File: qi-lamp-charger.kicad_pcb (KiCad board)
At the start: 2 copper layers, 41.5 x 44 mm, 82 parts, among them J1 Conn_01x03, J2 Conn_01x02, J4 Conn_01x06, J5 Conn_01x03, Q1 BSS308PE H6327, SW1 SKTDLDE010, U1 SLG5NV1430V, U2 BQ51050BRHL, U3 ESP-12E

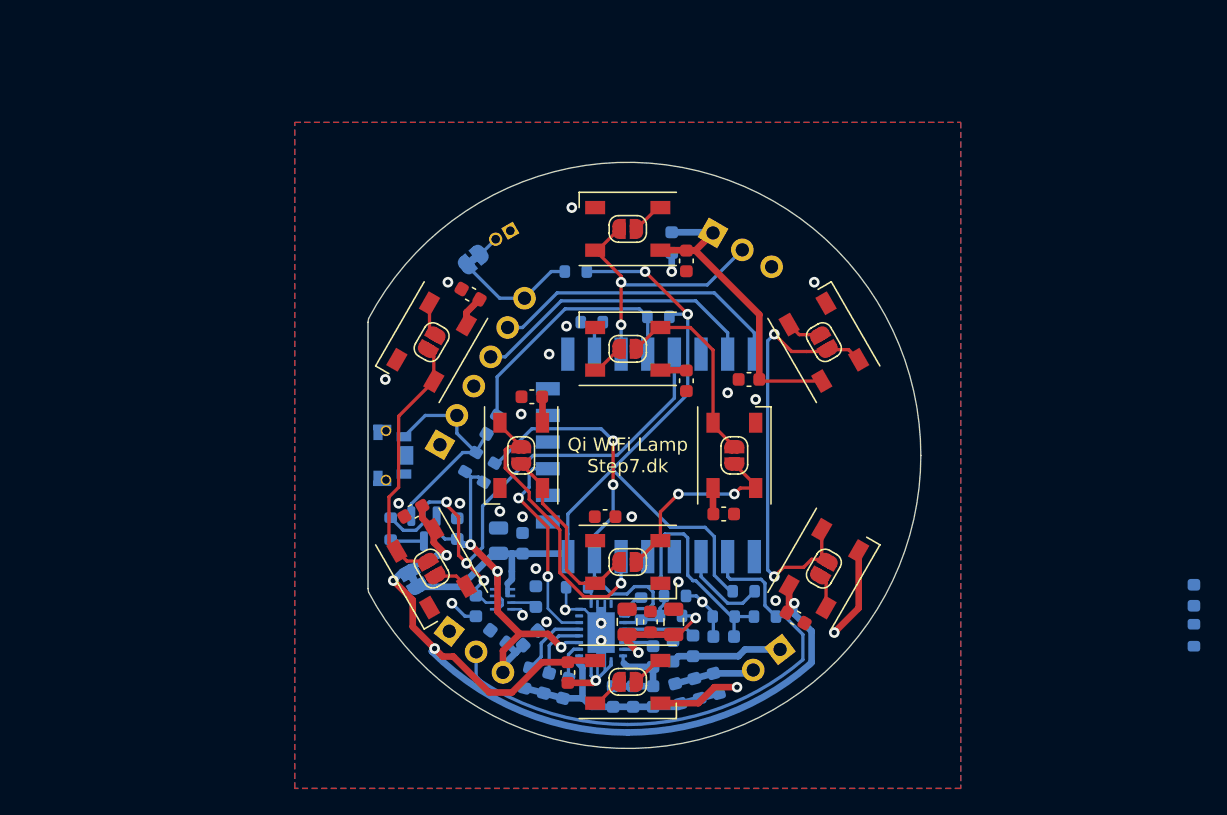
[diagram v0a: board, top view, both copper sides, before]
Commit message: Puzzle #4 - has GPIO0 brainfart
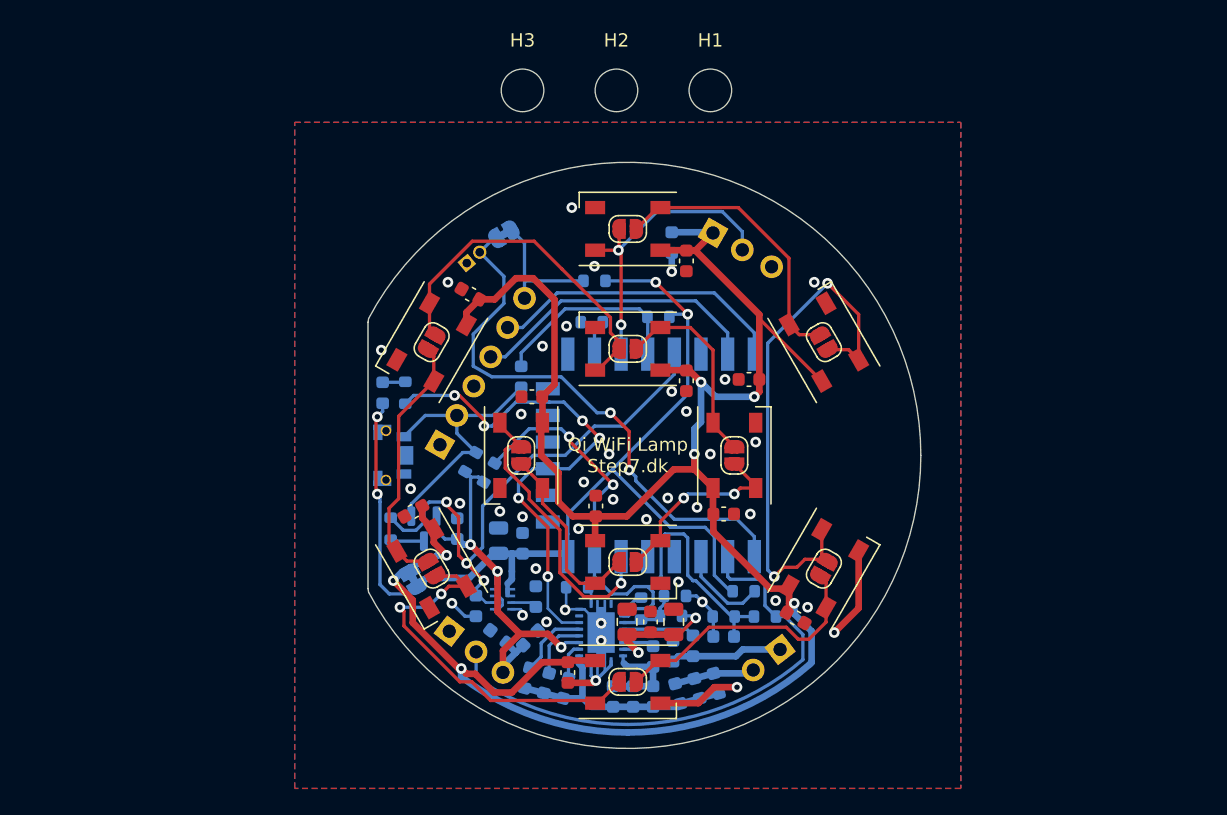
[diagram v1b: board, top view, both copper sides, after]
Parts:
- added H1: MountingHole, MountingHole:MountingHole_3.2mm_M3_ISO14580, F.Cu at (106.2, 72.6)
- added H2: MountingHole, MountingHole:MountingHole_3.2mm_M3_ISO14580, F.Cu at (99.2, 72.6)
- added H3: MountingHole, MountingHole:MountingHole_3.2mm_M3_ISO14580, F.Cu at (92.1, 72.6)
- moved D11 62.8 mm to (81.6, 95.3), turned to -90 degrees
- moved R4 61.9 mm to (83.3, 95.3)
- moved D12 4.22 mm to (92.0, 94.1), turned to 90 degrees
- moved TP1 4.07 mm to (87.9, 85.6), turned to -50 degrees
- moved JP12 2.98 mm to (90.7, 83.4), turned to 30 degrees
- moved R10 1.57 mm to (97.5, 86.9)
- moved C32 1.06 mm to (97.6, 103.8), turned to -90 degrees
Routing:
- net LED_V+: track 101.3 -> 160.8 mm, vias 4 -> 7
- net ~{ESP_RST}: track 1.65 -> 41.7 mm, vias 0 -> 2
- net Net-(D4-Pad4): track 5.06 -> 29.0 mm, vias 0 -> 2
- net ~{Qi_CHG/LED}: track 15.8 -> 38.6 mm, vias 2 -> 6
- net Net-(D6-Pad4): track 5.02 -> 26.4 mm
- net Net-(D1-Pad4): track 5.06 -> 21.3 mm
- net +VSW: track 62.3 -> 77.9 mm, vias 2 -> 4
- net Net-(D3-Pad4): track 5.02 -> 20.5 mm
- net Net-(D2-Pad4): track 33.1 -> 40.6 mm
- net ESP_GPIO0: track 19.4 -> 14.9 mm
- net DTR: track 17.0 -> 21.1 mm
- net LED_DIN: track 21.3 -> 23.7 mm
- net Net-(D11-Pad1): track 0.00 -> 1.72 mm
- net Qi_TS/CTRL: track 47.0 -> 45.4 mm
- net PWR_ON/~{OFF}: track 42.0 -> 40.9 mm
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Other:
- board text added: "GND DTR n/c TXD RXD RTS"
- board text added: "GND D_{in} V+"

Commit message: Puzzle #5
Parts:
- R10, R11, R12, R13, R9: value 10k -> 20k
- R14: value 1M -> 20k
- moved J5 5.11 mm to (110.8, 85.9), turned to 60 degrees
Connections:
- J5 pad 1: LED_V+ -> GND
- J5 pad 3: GND -> LED_V+
- Q1 pad 1: DTR -> BTN
- R14 pad 1: DTR -> BTN
- SW1 pad 2: DTR -> BTN
- U3 pad 5: unconnected-(U3-Pad5) -> BTN
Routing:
- net DTR: track 21.1 -> 5.71 mm
- net BTN: track 0.00 -> 13.9 mm
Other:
- board text added: "r${REVISION} Qi WiFi Lamp Step7.dk Martin Axelsen"
- board text removed: "Qi WiFi Lamp Step7.dk"
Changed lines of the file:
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@@
   )
   (paper "A4")
+  (title_block
+    (date "2022-05-20")
+    (rev "1.0.0")
+  )
   (layers
     (0 "F.Cu" signal)
@@
   (net 40 "Net-(R13-Pad2)")
   (net 41 "unconnected-(U3-Pad4)")
-  (net 42 "unconnected-(U3-Pad5)")
+  (net 42 "BTN")
   (net 43 "unconnected-(U3-Pad9)")
   (net 44 "unconnected-(U3-Pad10)")
@@
       (effects (font (size 1 1) (thickness 0.15)) (justify mirror))
     )
-    (fp_text value "10k" (at 0 -1.43) (layer "B.Fab") hide
+    (fp_text value "20k" (at 0 -1.43) (layer "B.Fab") hide
       (effects (font (size 1 1) (thickness 0.15)) (justify mirror))
     )
@@
       (net 41 "unconnected-(U3-Pad4)") (pinfunction "GPIO16") (pintype "bidirectional+no_connect"))
     (pad "5" smd rect (at -7.6 -4.5 90) (size 2.5 1) (layers "B.Cu" "B.Paste" "B.Mask")
-      (net 42 "unconnected-(U3-Pad5)") (pinfunction "GPIO14") (pintype "bidirectional+no_connect"))
+      (net 42 "BTN") (pinfunction "GPIO14") (pintype "bidirectional"))
     (pad "6" smd rect (at -7.6 -6.5 90) (size 2.5 1) (layers "B.Cu" "B.Paste" "B.Mask")
       (net 28 "LED_DOUT") (pinfunction "GPIO12") (pintype "bidirectional"))
@@
   )
   (footprint "Connector_PinHeader_2.54mm:PinHeader_1x03_P2.54mm_Vertical" (layer "B.Cu")
-    (at 106.4 83.3 -120)
+    (at 110.8 85.9 60)
     (descr "Through hole straight pin header, 1x03, 2.54mm pitch, single row")
     (tags "Through hole pin header THT 1x03 2.54mm single row")
@@
       (effects (font (size 1 1) (thickness 0.15)) (justify mirror))
     )
-    (fp_text user "Ext.LED" (at -3.001666 -2.539039 -30) (layer "B.SilkS")
+    (fp_text user "Ext.LED" (at 3.251666 -2.10795 150) (layer "B.SilkS")
       (effects (font (size 1 1) (thickness 0.15)) (justify mirror))
     )
@@
     (fp_line (start 1.27 -6.35) (end -1.27 -6.35) (layer "B.Fab") (width 0.1))
     (fp_line (start -0.635 1.27) (end 1.27 1.27) (layer "B.Fab") (width 0.1))
-    (pad "1" thru_hole rect (at 0 0 240) (size 1.7 1.7) (drill 1) (layers *.Cu *.Mask)
-      (net 23 "LED_V+") (pinfunction "Pin_1") (pintype "passive"))
-    (pad "2" thru_hole oval (at 0 -2.54 240) (size 1.7 1.7) (drill 1) (layers *.Cu *.Mask)
+    (pad "1" thru_hole rect (at 0 0 60) (size 1.7 1.7) (drill 1) (layers *.Cu *.Mask)
+      (net 5 "GND") (pinfunction "Pin_1") (pintype "passive"))
+    (pad "2" thru_hole oval (at 0 -2.54 60) (size 1.7 1.7) (drill 1) (layers *.Cu *.Mask)
       (net 24 "LED_DIN") (pinfunction "Pin_2") (pintype "passive"))
-    (pad "3" thru_hole oval (at 0 -5.08 240) (size 1.7 1.7) (drill 1) (layers *.Cu *.Mask)
-      (net 5 "GND") (pinfunction "Pin_3") (pintype "passive"))
+    (pad "3" thru_hole oval (at 0 -5.08 60) (size 1.7 1.7) (drill 1) (layers *.Cu *.Mask)
+      (net 23 "LED_V+") (pinfunction "Pin_3") (pintype "passive"))
     (model "${KICAD6_3DMODEL_DIR}/Connector_PinHeader_2.54mm.3dshapes/PinHeader_1x03_P2.54mm_Vertical.wrl" hide
       (offset (xyz 0 0 0))
@@
       (effects (font (size 1 1) (thickness 0.15)) (justify mirror))
     )
-    (fp_text value "10k" (at 0 -1.43) (layer "B.Fab") hide
+    (fp_text value "20k" (at 0 -1.43) (layer "B.Fab") hide
       (effects (font (size 1 1) (thickness 0.15)) (justify mirror))
     )
@@
       (effects (font (size 1 1) (thickness 0.15)) (justify mirror))
     )
-    (fp_text value "10k" (at 0 -1.43 90) (layer "B.Fab") hide
+    (fp_text value "20k" (at 0 -1.43 90) (layer "B.Fab") hide
       (effects (font (size 1 1) (thickness 0.15)) (justify mirror))
     )
@@
       (effects (font (size 1 1) (thickness 0.15)) (justify mirror))
     )
-    (fp_text value "10k" (at 0 -1.43) (layer "B.Fab") hide
+    (fp_text value "20k" (at 0 -1.43) (layer "B.Fab") hide
       (effects (font (size 1 1) (thickness 0.15)) (justify mirror))
     )
@@
       (net 5 "GND") (pinfunction "1") (pintype "passive"))
     (pad "2" smd rect locked (at 1.4 1.35 90) (size 0.7 1.1) (layers "B.Cu" "B.Paste" "B.Mask")
-      (net 29 "DTR") (pinfunction "2") (pintype "passive"))
+      (net 42 "BTN") (pinfunction "2") (pintype "passive"))
     (pad "3" smd rect locked (at 0 1.5 90) (size 1.4 1.1) (layers "B.Cu" "B.Paste" "B.Mask")
       (net 5 "GND") (pintype "passive"))
@@
       (effects (font (size 1 1) (thickness 0.15)) (justify mirror))
     )
-    (fp_text value "1M" (at 0 -1.43 60) (layer "B.Fab") hide
+    (fp_text value "20k" (at 0 -1.43 60) (layer "B.Fab") hide
       (effects (font (size 1 1) (thickness 0.15)) (justify mirror))
     )
@@
     (fp_line (start -0.8 -0.4125) (end -0.8 0.4125) (layer "B.Fab") (width 0.1))
     (pad "1" smd roundrect (at -0.825 0 240) (size 0.8 0.95) (layers "B.Cu" "B.Paste" "B.Mask") (roundrect_rratio 0.25)
-      (net 29 "DTR") (pintype "passive"))
+      (net 42 "BTN") (pintype "passive"))
     (pad "2" smd roundrect (at 0.825 0 240) (size 0.8 0.95) (layers "B.Cu" "B.Paste" "B.Mask") (roundrect_rratio 0.25)
       (net 6 "+BATT") (pintype "passive"))
@@
       (effects (font (size 1 1) (thickness 0.15)) (justify mirror))
     )
-    (fp_text value "10k" (at 0 -1.43) (layer "B.Fab") hide
+    (fp_text value "20k" (at 0 -1.43) (layer "B.Fab") hide
       (effects (font (size 1 1) (thickness 0.15)) (justify mirror))
     )
@@
     (fp_line (start 0.65 1.45) (end 0.65 -1.45) (layer "B.Fab") (width 0.1))
     (pad "1" smd roundrect (at -0.9375 0.95 270) (size 1.475 0.6) (layers "B.Cu" "B.Paste" "B.Mask") (roundrect_rratio 0.25)
-      (net 29 "DTR") (pinfunction "G") (pintype "input"))
+      (net 42 "BTN") (pinfunction "G") (pintype "input"))
     (pad "2" smd roundrect (at -0.9375 -0.95 270) (size 1.475 0.6) (layers "B.Cu" "B.Paste" "B.Mask") (roundrect_rratio 0.25)
       (net 6 "+BATT") (pinfunction "S") (pintype "passive"))
@@
     (effects (font (size 1 1) (thickness 0.15)) (justify mirror))
   )
-  (gr_text "Qi WiFi Lamp\nStep7.dk" (at 100 100) (layer "F.SilkS")
+  (gr_text "r${REVISION}\nQi WiFi Lamp\nStep7.dk\n\nMartin Axelsen" (at 115.75 100 270) (layer "F.SilkS")
     (effects (font (size 1 1) (thickness 0.15)))
   )
@@
   (via (at 99.5 109.6) (size 0.8) (drill 0.4) (layers "F.Cu" "B.Cu") (net 28))
   (segment (start 99.5 109.6) (end 99.5 107.6) (width 0.25) (layer "B.Cu") (net 28))
-  (segment (start 83.75 103.65) (end 83.75 104.5625) (width 0.25) (layer "B.Cu") (net 29))
-  (segment (start 87.17 98.343029) (end 88.6125 99.785529) (width 0.25) (layer "B.Cu") (net 29))
   (segment (start 89.887205 97.000295) (end 87.17 97.000295) (width 0.25) (layer "B.Cu") (net 29))
   (segment (start 92 94.8875) (end 89.887205 97.000295) (width 0.25) (layer "B.Cu") (net 29))
-  (segment (start 88.6125 99.785529) (end 87.614471 99.785529) (width 0.25) (layer "B.Cu") (net 29))
-  (segment (start 87.17 97.000295) (end 84.799705 97.000295) (width 0.25) (layer "B.Cu") (net 29))
-  (segment (start 87.614471 99.785529) (end 83.75 103.65) (width 0.25) (layer "B.Cu") (net 29))
-  (segment (start 84.799705 97.000295) (end 83.2 98.6) (width 0.25) (layer "B.Cu") (net 29))
-  (segment (start 87.17 97.000295) (end 87.17 98.343029) (width 0.25) (layer "B.Cu") (net 29))
   (segment (start 92 92.3) (end 92 93.3125) (width 0.25) (layer "B.Cu") (net 30))
   (segment (start 101.5 89.625) (end 101.475 89.6) (width 0.25) (layer "B.Cu") (net 30))
@@
   (segment (start 97.5 90.625) (end 98.125 90) (width 0.25) (layer "B.Cu") (net 40))
   (segment (start 97.5 92.4) (end 97.5 90.625) (width 0.25) (layer "B.Cu") (net 40))
+  (segment (start 83.75 103.65) (end 83.75 104.5625) (width 0.25) (layer "B.Cu") (net 42))
+  (segment (start 83.2 98.6) (end 84.2 97.6) (width 0.25) (layer "B.Cu") (net 42))
+  (segment (start 84.2 97.6) (end 85.5 97.6) (width 0.25) (layer "B.Cu") (net 42))
+  (segment (start 88.6125 99.785529) (end 88.585529 99.785529) (width 0.25) (layer "B.Cu") (net 42))
+  (segment (start 85.5 97.6) (end 87.3 98.5) (width 0.25) (layer "B.Cu") (net 42))
+  (segment (start 88.6125 99.785529) (end 87.614471 99.785529) (width 0.25) (layer "B.Cu") (net 42))
+  (segment (start 87.614471 99.785529) (end 83.75 103.65) (width 0.25) (layer "B.Cu") (net 42))
+  (segment (start 88.585529 99.785529) (end 87.3 98.5) (width 0.25) (layer "B.Cu") (net 42))
   (segment (start 100.1 98.2) (end 98.7 96.8) (width 0.25) (layer "F.Cu") (net 48))
   (segment (start 100.1 101.1) (end 100.1 98.2) (width 0.25) (layer "F.Cu") (net 48))
